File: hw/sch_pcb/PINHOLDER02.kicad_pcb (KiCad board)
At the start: 2 copper layers, 50.3 x 30 mm, 8 parts, among them J1 HEADER_1x03, M1 HOLE, M2 HOLE, M3 HOLE, M4 HOLE

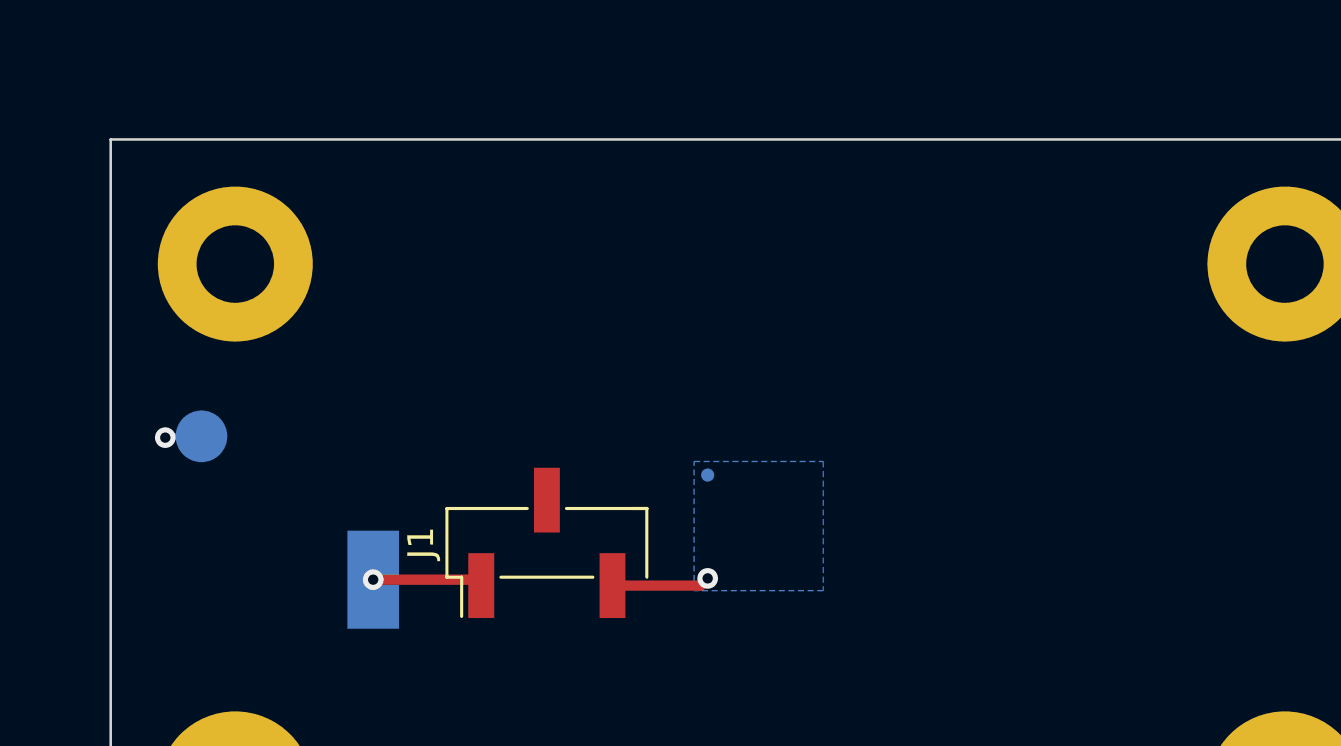
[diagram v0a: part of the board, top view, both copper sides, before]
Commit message: Cleanup layout. copy name to bottom.
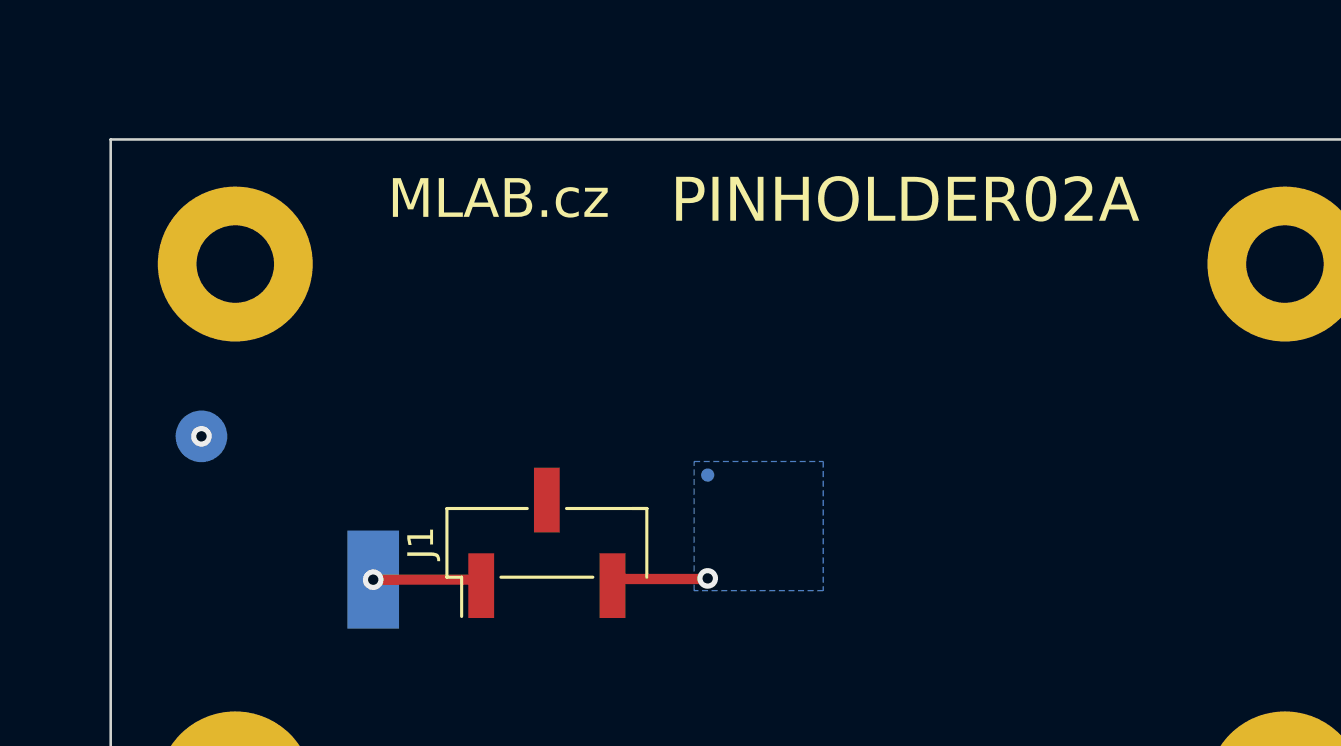
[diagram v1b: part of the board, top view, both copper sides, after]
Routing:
- net GND: track 1.42 -> 0.00 mm
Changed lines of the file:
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@@
     (effects (font (size 1.5 1.5) (thickness 0.3)) (justify mirror))
   )
-  (segment (start 164.214 88.929) (end 167.621 88.929) (width 0.4) (layer "F.Cu") (net 1))
-  (segment (start 167.621 88.929) (end 167.9 88.65) (width 0.4) (layer "F.Cu") (net 1))
+  (gr_text "PINHOLDER02A" (at 175.5394 74.0156) (layer "F.SilkS")
+    (effects (font (size 1.7 1.7) (thickness 0.3)))
+  )
+  (gr_text "MLAB.cz" (at 159.8134 73.9581) (layer "F.SilkS")
+    (effects (font (size 1.5 1.5) (thickness 0.3)))
+  )
+  (segment (start 167.8786 88.6714) (end 167.9 88.65) (width 0.4) (layer "F.Cu") (net 1))
+  (segment (start 164.4716 88.6714) (end 167.8786 88.6714) (width 0.4) (layer "F.Cu") (net 1))
+  (segment (start 164.214 88.929) (end 164.4716 88.6714) (width 0.4) (layer "F.Cu") (net 1))
   (via (at 167.9 88.65) (size 0.8) (drill 0.4) (layers "F.Cu" "B.Cu") (net 1))
-  (via (at 146.9 83.2) (size 0.8) (drill 0.4) (layers "F.Cu" "B.Cu") (net 2))
-  (segment (start 146.9 83.2) (end 146.95 83.15) (width 0.25) (layer "B.Cu") (net 2))
-  (segment (start 146.95 83.15) (end 148.3 83.15) (width 0.25) (layer "B.Cu") (net 2))
+  (via (at 148.300002 83.15) (size 0.8) (drill 0.4) (layers "F.Cu" "B.Cu") (net 2))
+  (segment (start 148.3 83.15) (end 148.300002 83.15) (width 0.25) (layer "B.Cu") (net 2))
   (segment (start 158.905 88.7) (end 159.134 88.929) (width 0.4) (layer "F.Cu") (net 3))
   (segment (start 154.95 88.7) (end 158.905 88.7) (width 0.4) (layer "F.Cu") (net 3))
